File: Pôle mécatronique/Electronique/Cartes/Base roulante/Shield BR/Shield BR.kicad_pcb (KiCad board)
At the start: 2 copper layers, 65 x 53 mm, 24 parts, among them J0 Conn_01x04_Female, J1 Conn_01x04_Female, J2 Conn_01x04_Female, J3 Conn_01x04_Female, J4 Conn_01x04_Male, J5 Conn_01x02_Female, SW1 SW_DIP_x04, SW2 SW_Push_SPDT, U4 R-78E5.0-0.5

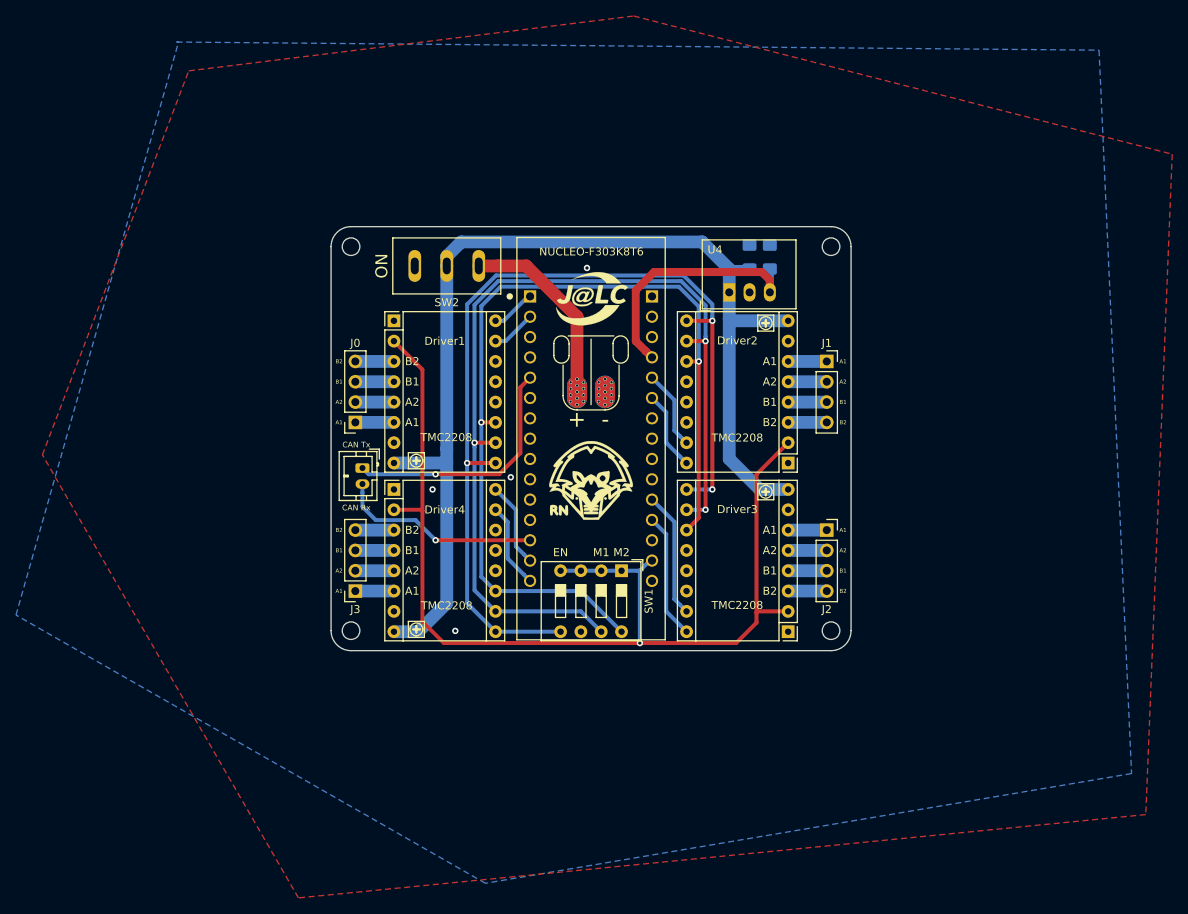
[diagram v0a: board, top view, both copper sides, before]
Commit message: Update BR et alim
- Mise à jour BR pour 2022 (taille de piste, modèle 3D ...)

- Changements mineurs sur l'alim
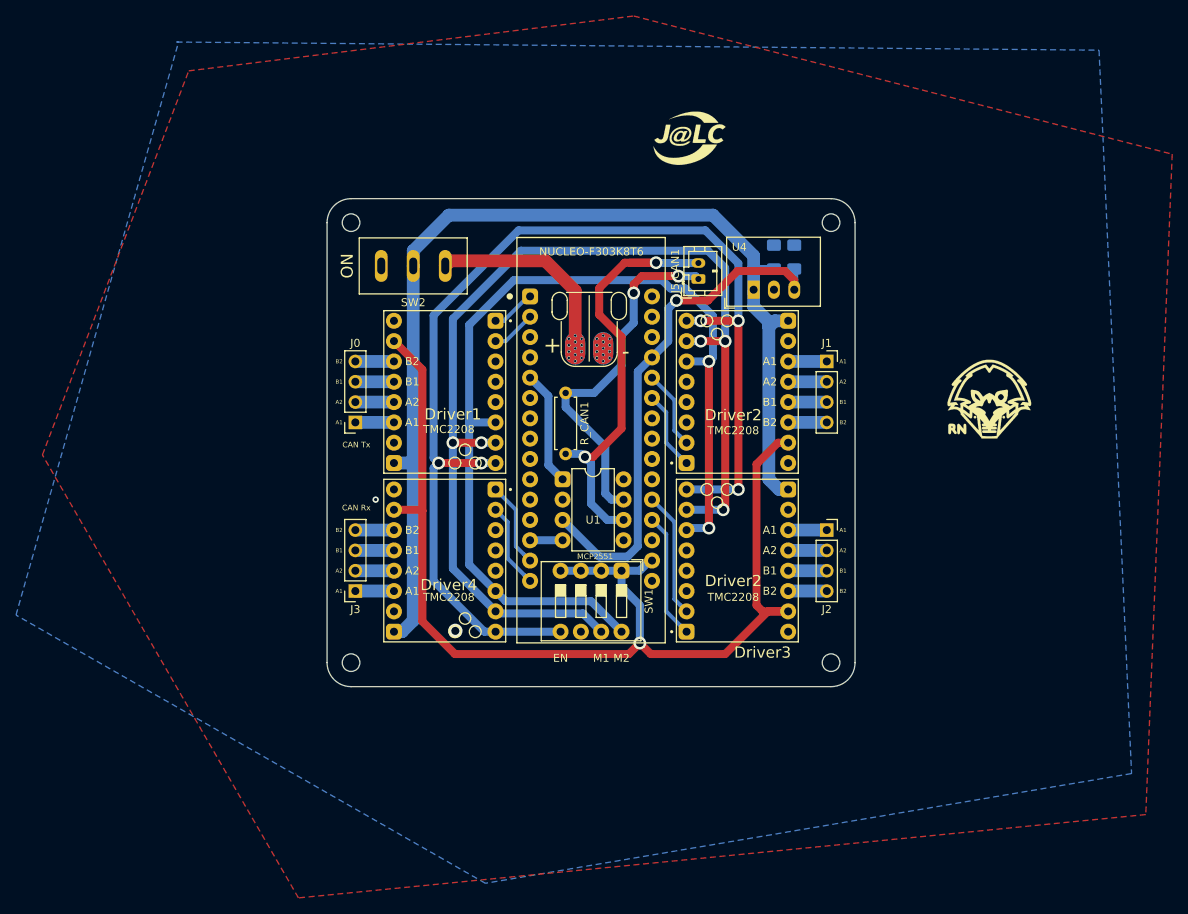
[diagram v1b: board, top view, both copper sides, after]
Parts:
- removed J5: Conn_01x02_Female, Connector_JST:JST_PH_B2B-PH-K_1x02_P2.00mm_Vertical
- added J5-CAN1: Conn_01x02_Female, Connector_JST:JST_PH_B2B-PH-K_1x02_P2.00mm_Vertical, F.Cu at (124.7, 73.8)
- added R_CAN1: R, Resistor_THT:R_Axial_DIN0207_L6.3mm_D2.5mm_P7.62mm_Horizontal, F.Cu at (108.1, 88.0)
- added U1: MCP2551, Package_DIP:DIP-8_W7.62mm, F.Cu at (107.7, 98.8)
- Driver1, Driver2, Driver3, Driver4: footprint Trinamic_Drivers:TMC_2208_BOB -> Autre:MODULE_TMC2208_SILENTSTEPSTICK
- moved G*** 67.6 mm to (178.8, 95.8)
- moved G*** 50.8 mm to (161.0, 88.6)
- moved G*** 24.7 mm to (59.9, 72.4)
- moved G*** 23.5 mm to (123.4, 55.9)
- moved J4 5.45 mm to (111.0, 82.4)
- moved SW2 4.19 mm to (89.0, 72.1)
- moved H2 4.00 mm to (141.3, 121.7)
- moved H3 4.00 mm to (81.3, 121.7)
- moved U4 3.07 mm to (131.6, 75.1)
- moved C0 3.05 mm to (134.1, 71.0)
- moved C1 3.05 mm to (136.7, 71.0)
- moved H0 3.00 mm to (81.3, 66.7)
- moved H1 3.00 mm to (141.3, 66.7)
- turned Driver1 to 0 degrees
- turned Driver2 to 180 degrees
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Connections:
- Driver1 pad 11: Net-(Driver1-Pad11) -> unconnected-(Driver1-Pad11)
- Driver1 pad 12: Net-(Driver1-Pad12) -> unconnected-(Driver1-Pad12)
- Driver1 pad 13: Net-(Driver1-Pad13) -> unconnected-(Driver1-Pad13)
- Driver2 pad 11: Net-(Driver2-Pad11) -> unconnected-(Driver2-Pad11)
- Driver2 pad 12: Net-(Driver2-Pad12) -> unconnected-(Driver2-Pad12)
- Driver2 pad 13: Net-(Driver2-Pad13) -> unconnected-(Driver2-Pad13)
- Driver3 pad 11: Net-(Driver3-Pad11) -> unconnected-(Driver3-Pad11)
- Driver3 pad 12: Net-(Driver3-Pad12) -> unconnected-(Driver3-Pad12)
- Driver3 pad 13: Net-(Driver3-Pad13) -> unconnected-(Driver3-Pad13)
- Driver4 pad 11: Net-(Driver4-Pad11) -> unconnected-(Driver4-Pad11)
- Driver4 pad 12: Net-(Driver4-Pad12) -> unconnected-(Driver4-Pad12)
- Driver4 pad 13: Net-(Driver4-Pad13) -> unconnected-(Driver4-Pad13)
- NUCLEO-F303K8T6 pad 3.10: Net-(NUCLEO-F303K8T6-Pad3.10) -> unconnected-(NUCLEO-F303K8T6-Pad3.10)
- NUCLEO-F303K8T6 pad 3.11: Net-(NUCLEO-F303K8T6-Pad3.11) -> unconnected-(NUCLEO-F303K8T6-Pad3.11)
- NUCLEO-F303K8T6 pad 3.12: Net-(NUCLEO-F303K8T6-Pad3.12) -> unconnected-(NUCLEO-F303K8T6-Pad3.12)
- NUCLEO-F303K8T6 pad 3.3: Net-(NUCLEO-F303K8T6-Pad3.3) -> unconnected-(NUCLEO-F303K8T6-Pad3.3)
- NUCLEO-F303K8T6 pad 3.6: Net-(NUCLEO-F303K8T6-Pad3.6) -> unconnected-(NUCLEO-F303K8T6-Pad3.6)
- NUCLEO-F303K8T6 pad 3.7: Net-(NUCLEO-F303K8T6-Pad3.7) -> unconnected-(NUCLEO-F303K8T6-Pad3.7)
- NUCLEO-F303K8T6 pad 3.8: Net-(NUCLEO-F303K8T6-Pad3.8) -> unconnected-(NUCLEO-F303K8T6-Pad3.8)
- NUCLEO-F303K8T6 pad 3.9: Net-(NUCLEO-F303K8T6-Pad3.9) -> unconnected-(NUCLEO-F303K8T6-Pad3.9)
- NUCLEO-F303K8T6 pad 4.1: Net-(NUCLEO-F303K8T6-Pad4.1) -> unconnected-(NUCLEO-F303K8T6-Pad4.1)
- NUCLEO-F303K8T6 pad 4.10: Net-(NUCLEO-F303K8T6-Pad4.10) -> unconnected-(NUCLEO-F303K8T6-Pad4.10)
- NUCLEO-F303K8T6 pad 4.13: Net-(NUCLEO-F303K8T6-Pad4.13) -> unconnected-(NUCLEO-F303K8T6-Pad4.13)
- NUCLEO-F303K8T6 pad 4.15: Net-(NUCLEO-F303K8T6-Pad4.15) -> unconnected-(NUCLEO-F303K8T6-Pad4.15)
- NUCLEO-F303K8T6 pad 4.3: Net-(NUCLEO-F303K8T6-Pad4.3) -> unconnected-(NUCLEO-F303K8T6-Pad4.3)
- NUCLEO-F303K8T6 pad 4.7: Net-(NUCLEO-F303K8T6-Pad4.7) -> unconnected-(NUCLEO-F303K8T6-Pad4.7)
- NUCLEO-F303K8T6 pad 4.8: Net-(NUCLEO-F303K8T6-Pad4.8) -> unconnected-(NUCLEO-F303K8T6-Pad4.8)
- NUCLEO-F303K8T6 pad 4.9: Net-(NUCLEO-F303K8T6-Pad4.9) -> unconnected-(NUCLEO-F303K8T6-Pad4.9)
- SW1 pad 6: Net-(SW1-Pad6) -> unconnected-(SW1-Pad6)
- SW2 pad 3: Net-(SW2-Pad3) -> unconnected-(SW2-Pad3)
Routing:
- net Net-(J5-CAN1-Pad2): track 0.00 -> 55.4 mm, vias 0 -> 2
- net Net-(J5-CAN1-Pad1): track 0.00 -> 45.1 mm, vias 0 -> 2
- net +5V: track 31.8 -> 65.7 mm, vias 0 -> 1
- net EN: track 117.3 -> 144.8 mm, vias 3 -> 5
- net CAN_Rx: track 25.5 -> 4.06 mm, vias 1 -> 0
- net M1: track 117.9 -> 136.6 mm, vias 3 -> 5
- net CAN_Tx: track 31.1 -> 14.4 mm, vias 1 -> 0
- net M2: track 115.3 -> 122.9 mm
- net Vio: track 133.2 -> 139.5 mm
- net +BATT: track 138.2 -> 135.1 mm
- net Net-(J4-Pad1): track 25.9 -> 26.9 mm
- net GND: vias 17 -> 15
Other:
- board size 65 x 53 mm -> 66 x 61 mm
- board text added: "Carte Base Roulante"
- board text added: "Driver2"
- board text removed: "Carte Prototype Base Roulante"
- board text removed: "Hugo Seigneur"
- board text removed: "Rx"
- board text removed: "Tx"

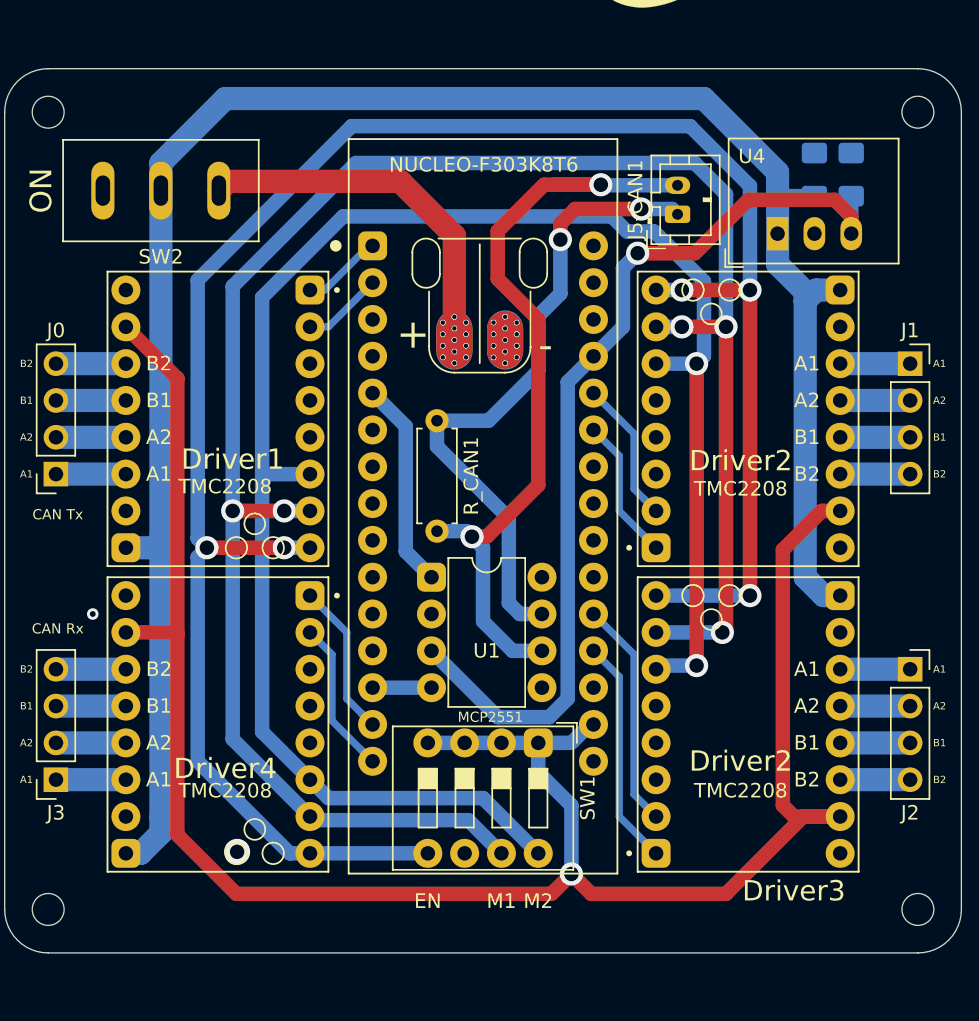
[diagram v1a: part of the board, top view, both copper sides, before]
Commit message: Update BR
- Avancement raccords EN/MS1/MS2
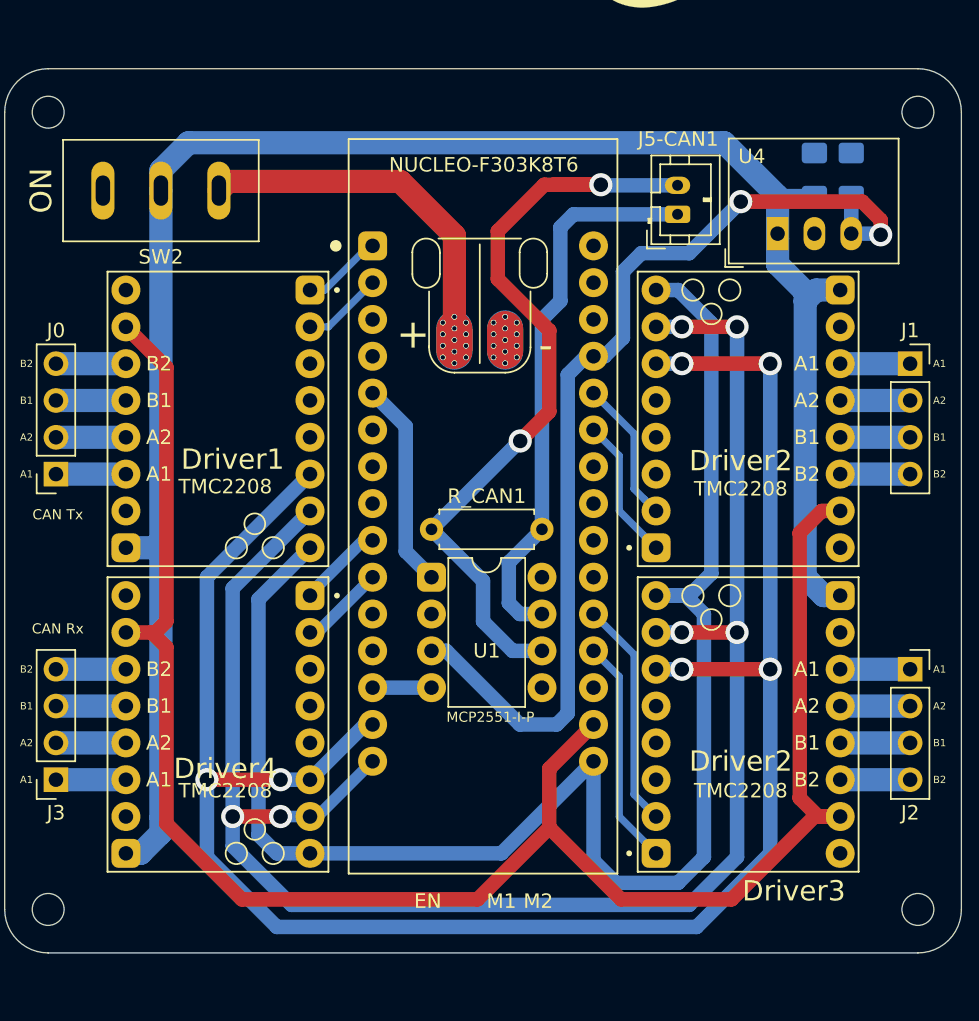
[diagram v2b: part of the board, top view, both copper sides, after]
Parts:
- removed SW1: SW_DIP_x04, Button_Switch_THT:SW_DIP_SPSTx04_Slide_9.78x12.34mm_W7.62mm_P2.54mm
- U1: value MCP2551 -> MCP2551-I-P
- moved R_CAN1 10.4 mm to (115.3, 95.5), turned to 180 degrees
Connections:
- NUCLEO-F303K8T6 pad 3.10: unconnected-(NUCLEO-F303K8T6-Pad3.10) -> Stp3
- NUCLEO-F303K8T6 pad 3.14: Dir3 -> M2
- NUCLEO-F303K8T6 pad 3.15: Stp3 -> M1
- NUCLEO-F303K8T6 pad 3.9: unconnected-(NUCLEO-F303K8T6-Pad3.9) -> Dir3
- NUCLEO-F303K8T6 pad 4.15: unconnected-(NUCLEO-F303K8T6-Pad4.15) -> EN
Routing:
- net EN: track 144.8 -> 110.5 mm, vias 5 -> 0
- net M1: track 136.6 -> 122.2 mm, vias 5 -> 6
- net Vio: track 139.5 -> 126.7 mm, vias 1 -> 0
- net M2: track 122.9 -> 134.9 mm, vias 2 -> 6
- net Net-(J5-CAN1-Pad1): track 45.1 -> 38.4 mm, vias 2 -> 0
- net +5V: track 65.7 -> 70.9 mm, vias 1 -> 2
- net Stp3: track 10.7 -> 5.90 mm
- net Dir3: track 10.7 -> 5.97 mm
- net +BATT: track 135.1 -> 131.3 mm
- net GND: vias 15 -> 13
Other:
- board text added: "CAN RX"
- board text added: "CAN TX"
- board text added: "CANH"
- board text added: "CANL"
- board text removed: "JLCJLCJLCJLC"
- board text removed: "PB4-Step4"
- board text removed: "PB5-Dir4"

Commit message: Updates mineurs
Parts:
- renumbered J5-CAN1 to J5-CAN, R_CAN1 to R_CAN
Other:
- board text removed: "CAN Rx"
- board text removed: "CAN Tx"
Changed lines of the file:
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@@
     (property "Sheetname" "")
     (attr through_hole)
-    (fp_text reference "R_CAN1" (at 3.81 2.286) (layer "F.SilkS")
+    (fp_text reference "R_CAN" (at 3.81 2.286) (layer "F.SilkS")
       (effects (font (size 1 1) (thickness 0.15)))
     )
@@
     (property "Sheetname" "")
     (attr through_hole)
-    (fp_text reference "J5-CAN1" (at 5.191 0.042 180) (layer "F.SilkS")
+    (fp_text reference "J5-CAN" (at 5.191 0.042 180) (layer "F.SilkS")
       (effects (font (size 1 1) (thickness 0.15)))
     )
@@
     (fp_line (start 6.985 -1.27) (end 6.985 8.89) (layer "F.Fab") (width 0.1))
     (fp_line (start 0.635 -0.27) (end 1.635 -1.27) (layer "F.Fab") (width 0.1))
-    (pad "1" thru_hole roundrect (at 0 0) (size 2 2) (drill 1) (layers *.Cu *.Mask) (roundrect_rratio 0.25)
+    (pad "1" thru_hole rect (at 0 0) (size 2 2) (drill 1) (layers *.Cu *.Mask)
       (net 7 "CAN_Tx") (pinfunction "TXD") (pintype "input"))
     (pad "2" thru_hole circle (at 0 2.54) (size 2 2) (drill 1) (layers *.Cu *.Mask)
@@
     (effects (font (size 1 1) (thickness 0.15)))
   )
-  (gr_text "CAN Rx" (at 81.9145 102.362) (layer "F.SilkS")
-    (effects (font (size 0.7 0.7) (thickness 0.1)))
-  )
   (gr_text "B1" (at 133.6035 89.154) (layer "F.SilkS")
     (effects (font (size 1 1) (thickness 0.15)))
@@
     (effects (font (size 2 2) (thickness 0.4)))
   )
-  (gr_text "CAN Tx" (at 81.9145 94.488) (layer "F.SilkS")
-    (effects (font (size 0.7 0.7) (thickness 0.1)))
-  )
   (gr_text "ON" (at 80.7715 72.136 90) (layer "F.SilkS")

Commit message: Update BR
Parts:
- removed the G*** at (123.4, 55.9)
- removed the G*** at (59.9, 72.4)
- moved G*** 71.5 mm to (111.0, 118.4)
- moved G*** 55.9 mm to (111.3, 114.0)
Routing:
- net Stp3: track 5.90 -> 6.49 mm
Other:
- board text added: "CAN_Rx"
- board text added: "VBATT"
- board text removed: "Dir1-PA9"
- board text removed: "PA0-Dir3"
- board text removed: "PA1-Step3"
- board text removed: "PA11-CAN_Rx"
- board text removed: "Step1-PA10"

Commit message: Update BR
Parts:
- removed C0: 10u, Capacitor_SMD:C_1206_3216Metric_Pad1.42x1.75mm_HandSolder
- added C2: 100pF, Capacitor_SMD:C_1206_3216Metric_Pad1.33x1.80mm_HandSolder, F.Cu at (111.4, 110.4)
- added C3: 10u, Capacitor_SMD:C_1206_3216Metric_Pad1.33x1.80mm_HandSolder, B.Cu at (133.9, 71.0)
- added C4: 10u, Capacitor_SMD:C_1206_3216Metric_Pad1.33x1.80mm_HandSolder, B.Cu at (136.7, 71.0)
- added C5: 100n, Capacitor_SMD:C_1206_3216Metric_Pad1.33x1.80mm_HandSolder, B.Cu at (139.2, 71.0)
- added C6: 220 à 1000 µF, Capacitor_THT:CP_Radial_D8.0mm_P3.50mm, F.Cu at (131.8, 113.8)
- added C7: 220 à 1000 µF, Capacitor_THT:CP_Radial_D8.0mm_P3.50mm, F.Cu at (90.9, 82.8)
- added C8: 220 à 1000 µF, Capacitor_THT:CP_Radial_D8.0mm_P3.50mm, F.Cu at (131.8, 91.9)
- added C9: 220 à 1000 µF, Capacitor_THT:CP_Radial_D8.0mm_P3.50mm, F.Cu at (90.9, 104.1)
- added REF**: TestPoint_Pad_D2.0mm, TestPoint:TestPoint_Pad_D2.0mm, B.Cu at (110.7, 106.2)
- added TP1: TestPoint, TestPoint:TestPoint_Pad_D2.0mm, B.Cu at (140.8, 74.5)
- added TP2: TestPoint, TestPoint:TestPoint_Pad_D2.0mm, B.Cu at (126.1, 68.2)
- added TP3: TestPoint, TestPoint:TestPoint_Pad_D2.0mm, B.Cu at (120.9, 73.9)
- added TP4: TestPoint, TestPoint:TestPoint_Pad_D2.0mm, B.Cu at (122.4, 71.6)
- added TP5: TestPoint, TestPoint:TestPoint_Pad_D2.0mm, B.Cu at (106.6, 93.1)
- added TP6: TestPoint, TestPoint:TestPoint_Pad_D2.0mm, B.Cu at (110.2, 112.3)
- added TP7: TestPoint, TestPoint:TestPoint_Pad_D2.0mm, B.Cu at (130.3, 119.4)
- added TP8: TestPoint, TestPoint:TestPoint_Pad_D2.0mm, B.Cu at (102.4, 120.1)
- added TP9: TestPoint, TestPoint:TestPoint_Pad_D2.0mm, B.Cu at (104.1, 117.7)
- C1: value 10u -> 100nF; footprint Capacitor_SMD:C_1206_3216Metric_Pad1.42x1.75mm_HandSolder -> Capacitor_SMD:C_1206_3216Metric_Pad1.33x1.80mm_HandSolder; moved to F.Cu
- moved C1 48.9 mm to (111.4, 112.9), turned to 180 degrees
- moved G*** 5.21 mm to (111.3, 119.3)
- moved R_CAN1 3.34 mm to (112.0, 96.0), turned to 90 degrees
- moved J1 1.33 mm to (111.0, 81.1)
- moved SW1 1.14 mm to (90.2, 72.1)
- renumbered Driver4 to Driver3, Driver3 to Driver4, H0 to H2, H2 to H4, J4 to J1, J0 to J2, J1 to J3, J3 to J4, J2 to J5, J5-CAN to J5-CAN1, NUCLEO-F303K8T6 to NUCLEO-F303K8T1, R_CAN to R_CAN1, SW2 to SW1, U4 to U1, U1 to U2
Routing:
- net +BATT: track 131.8 -> 151.8 mm
- net +5V: track 70.9 -> 83.3 mm, vias 2 -> 3
- net Net-(J5-CAN1-Pad2): track 55.2 -> 45.3 mm
- net CAN_Rx: track 4.06 -> 11.0 mm
- net M1: track 122.5 -> 125.1 mm
- net Net-(J1-Pad1): track 26.9 -> 25.1 mm
- net Vio: track 126.7 -> 124.9 mm
- net M2: track 135.2 -> 136.1 mm
- net Net-(J5-CAN1-Pad1): track 38.4 -> 39.3 mm
- net GND: vias 13 -> 20
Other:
- board text added: "1"
- board text added: "2"
- board text added: "3"
- board text added: "4"
- board text added: "CanH"
- board text added: "CanL"
- board text removed: "Driver2"
- board text removed: "Step1"
- board text removed: "TMC2208"
